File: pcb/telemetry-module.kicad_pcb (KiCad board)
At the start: 2 copper layers, 45.5 x 30 mm, 8 parts, among them J1 ODU Diagnostic Port, J3 5V-3.3V Level Shifter, J4 XIAO ESP32S3, J5 ODU 5V power jumper

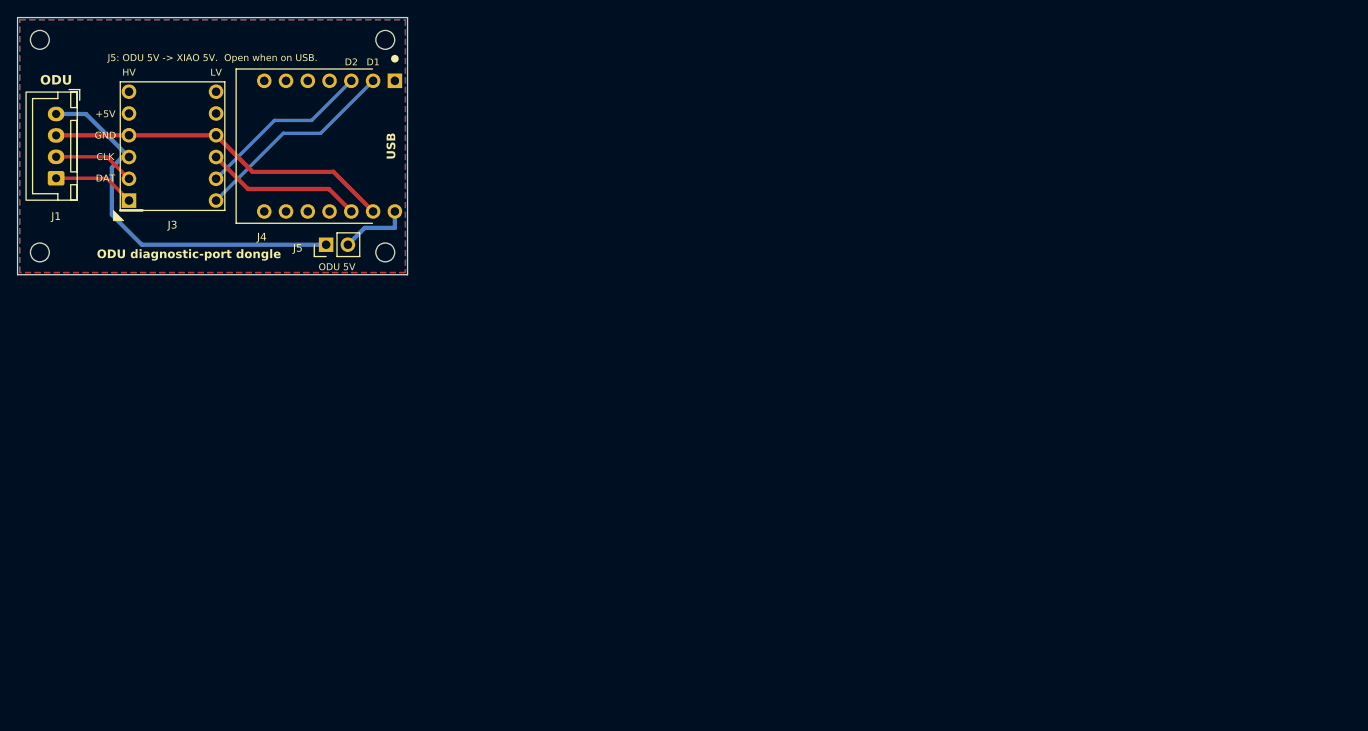
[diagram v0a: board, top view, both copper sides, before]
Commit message: GH-0014: reduce size of PCB
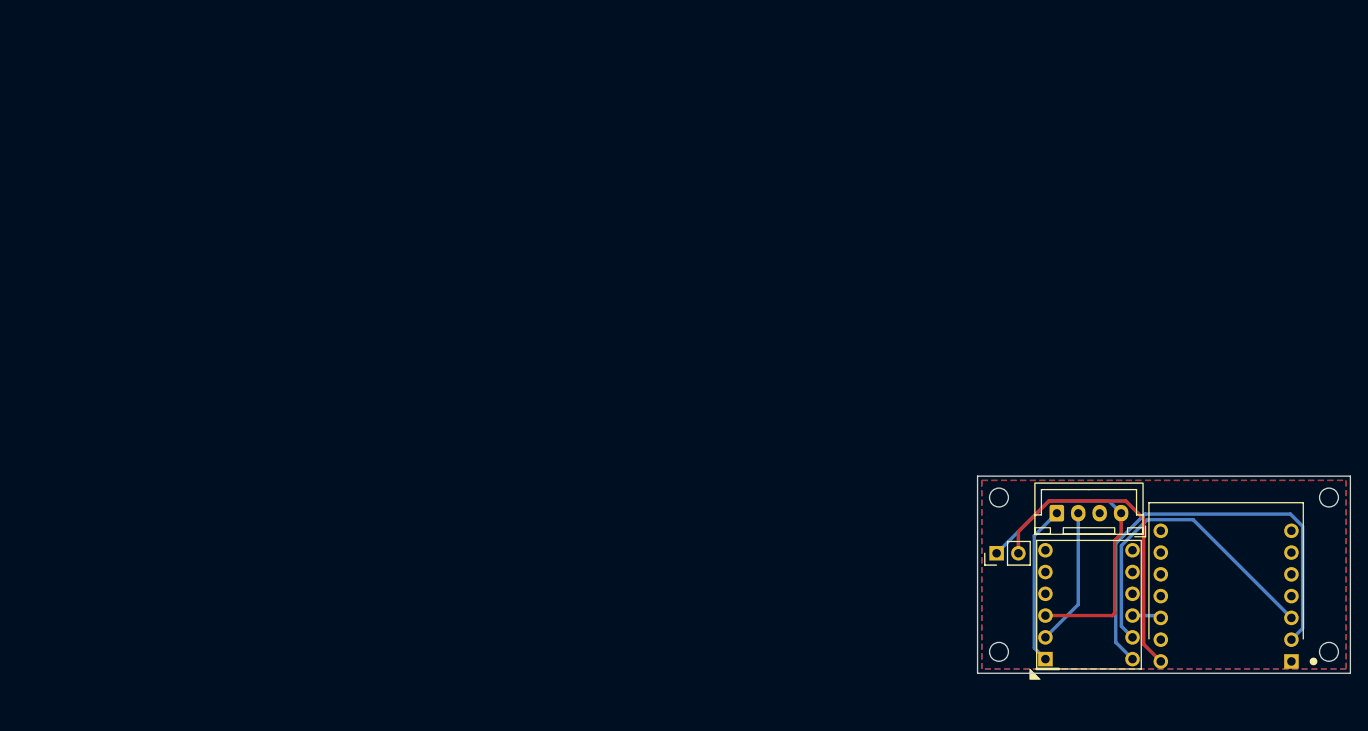
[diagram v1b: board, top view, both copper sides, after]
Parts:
- moved H1 124.0 mm to (114.5, 56.0)
- moved J1 123.1 mm to (121.2, 57.8), turned to 0 degrees
- moved H3 122.4 mm to (153.0, 56.0)
- moved H2 121.2 mm to (114.5, 74.0)
- moved J3 119.6 mm to (125.0, 68.5)
- moved H4 119.6 mm to (153.0, 74.0)
- moved J4 117.0 mm to (141.0, 67.5), turned to -90 degrees
- moved J5 86.1 mm to (114.2, 62.5)
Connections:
- net /GND renamed GND
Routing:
- net GND: track 40.7 -> 0.00 mm
- net /XIAO_5V: track 8.21 -> 36.9 mm
- net /DAT_3V3: track 24.1 -> 51.9 mm
- net /CLK_3V3: track 20.5 -> 37.1 mm
- net /+3V3: track 18.4 -> 3.41 mm
- net /DAT_5V: track 9.58 -> 18.7 mm
- net /ODU_5V: track 45.0 -> 37.8 mm
- net /CLK_5V: track 9.56 -> 16.1 mm
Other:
- board size 45.5 x 30 mm -> 43.5 x 23 mm
- board text removed: "+5V"
- board text removed: "CLK"
- board text removed: "D1"
- board text removed: "D2"
- board text removed: "DAT"
- board text removed: "GND"
- board text removed: "HV"
- board text removed: "J5: ODU 5V -> XIAO 5V. Open when on USB."
- board text removed: "LV"
- board text removed: "ODU"
- board text removed: "ODU 5V"
- board text removed: "ODU diagnostic-port dongle"
- board text removed: "USB"

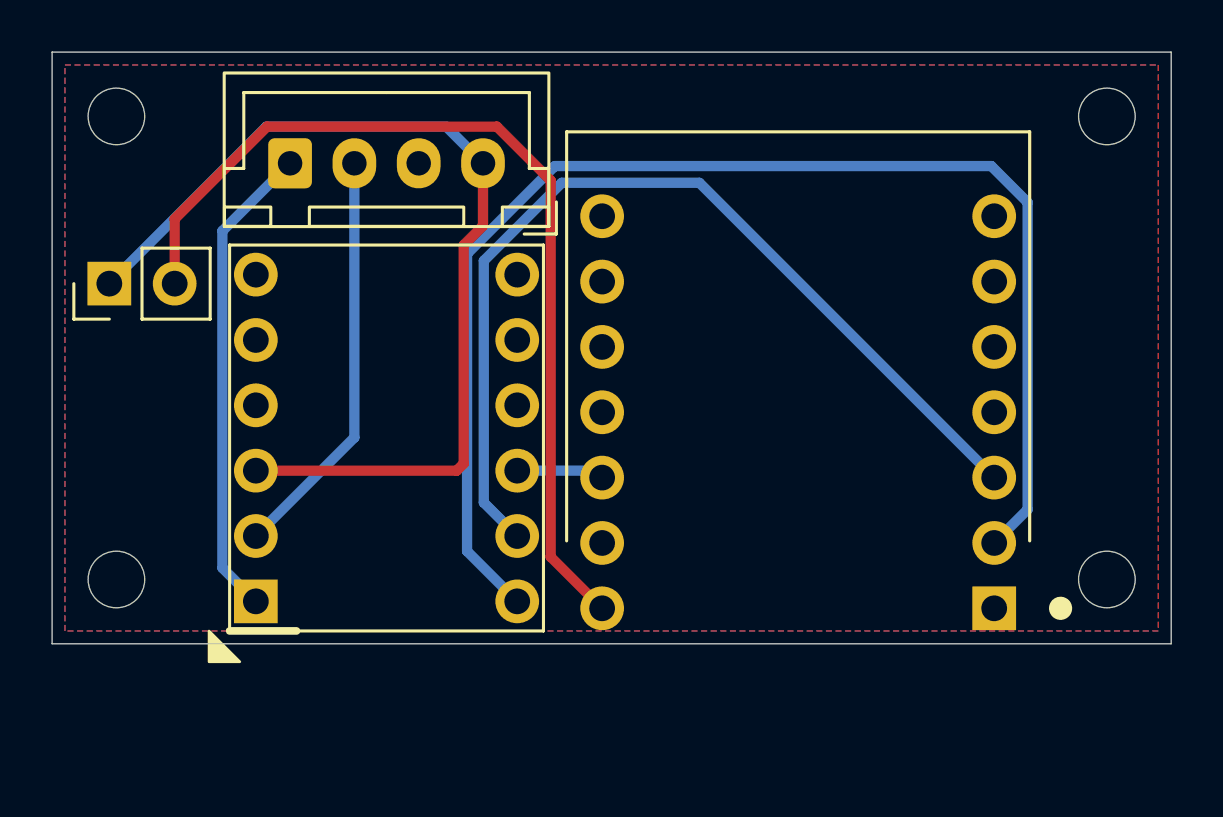
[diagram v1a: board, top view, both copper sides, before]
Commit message: GH-0014: reduce size of PCB
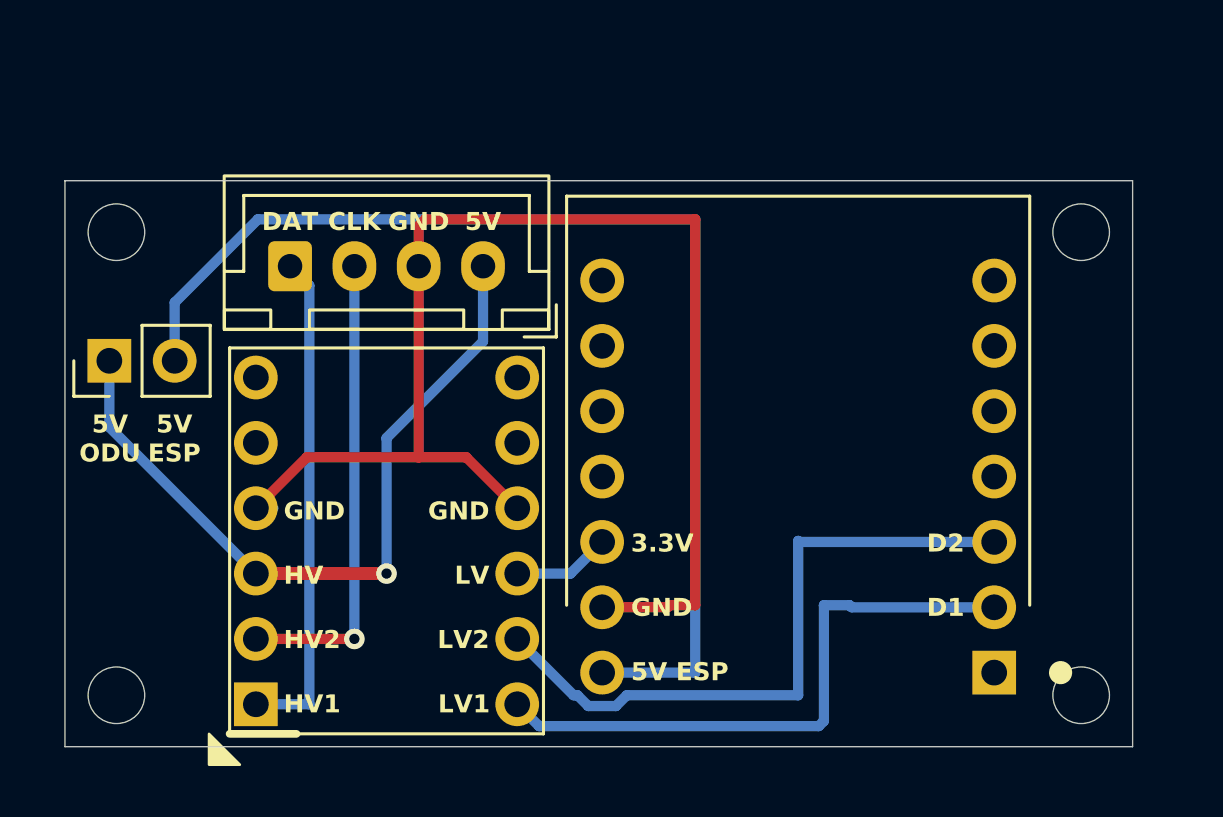
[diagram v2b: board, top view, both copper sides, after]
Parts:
- moved H3 4.61 mm to (152.0, 60.5)
- moved H4 4.61 mm to (152.0, 78.5)
- moved H1 4.50 mm to (114.5, 60.5)
- moved H2 4.50 mm to (114.5, 78.5)
- moved J1 4.00 mm to (121.2, 61.8)
- moved J3 4.00 mm to (125.0, 72.5)
- moved J5 3.00 mm to (114.2, 65.5)
- moved J4 2.50 mm to (141.0, 70.0)
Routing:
- net GND: track 0.00 -> 51.0 mm
- net /DAT_3V3: track 51.9 -> 23.5 mm
- net /CLK_3V3: track 37.1 -> 25.8 mm
- net /ODU_5V: track 37.8 -> 29.2 mm, vias 0 -> 1
- net /XIAO_5V: track 36.9 -> 45.1 mm
- net /CLK_5V: track 16.1 -> 18.3 mm, vias 0 -> 1
- net /DAT_5V: track 18.7 -> 19.4 mm
- removed copper zone on B.Cu, net GND
- removed copper zone on F.Cu, net GND
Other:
- board size 43.5 x 23 mm -> 41.5 x 22 mm
- board text added: "3.3V"
- board text added: "5V"
- board text added: "5V ESP"
- board text added: "5V ODU"
- board text added: "CLK"
- board text added: "D1"
- board text added: "D2"
- board text added: "DAT"
- board text added: "GND"
- board text added: "HV"
- board text added: "HV1"
- board text added: "HV2"
- board text added: "LV"
- board text added: "LV1"
- board text added: "LV2"
